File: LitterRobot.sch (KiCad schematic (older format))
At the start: 4 parts, among them J1 DF11C-4DP-2V(57), J2 Hirose_DF11C-6DP-2V(57), J3 DF11C-8DP-2V(57), J4 DF11C-10DP-2V(57)

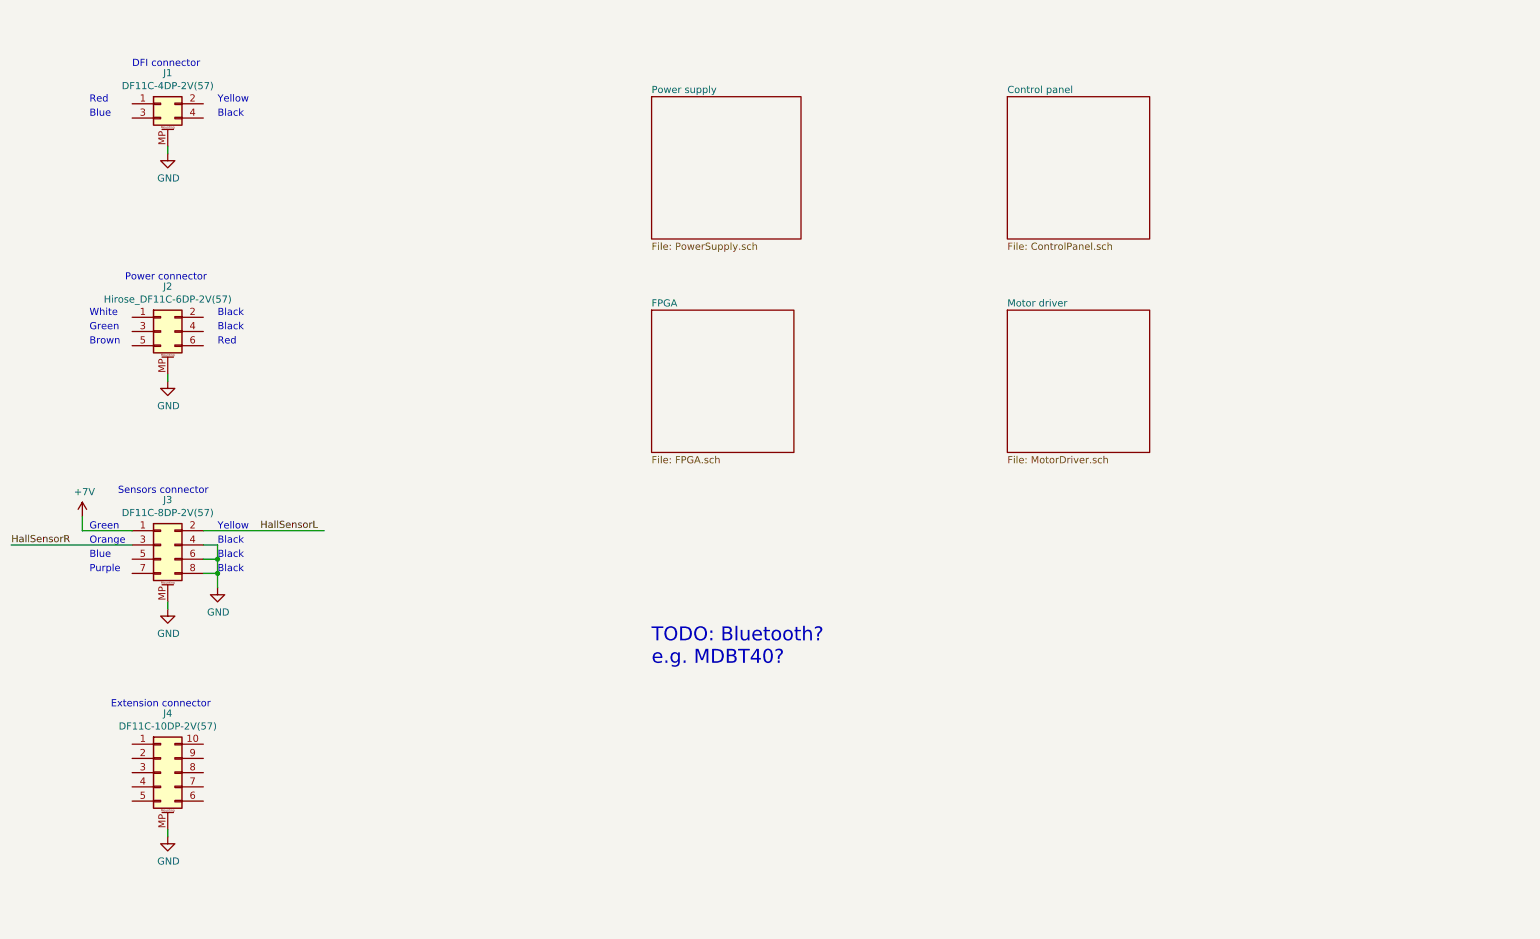
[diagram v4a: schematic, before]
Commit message: Add the power supply and motor driver ICs
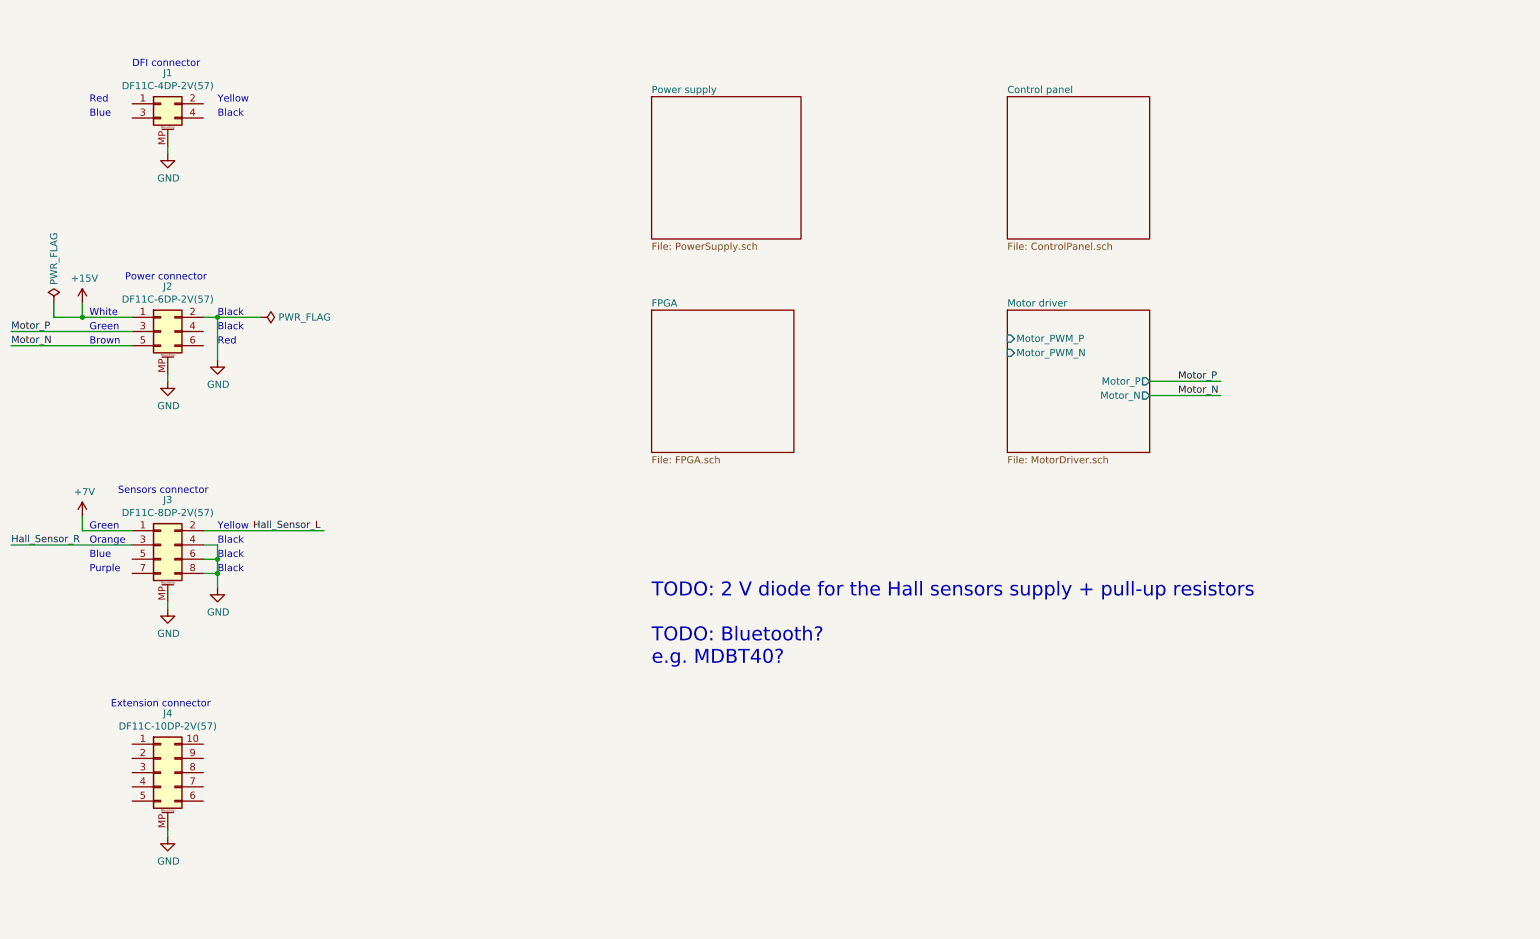
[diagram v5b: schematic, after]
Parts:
- J1: Part_Number (none) -> DF11C-4DP-2V(57)
- J2: value Hirose_DF11C-6DP-2V(57) -> DF11C-6DP-2V(57); Part_Number (none) -> DF11C-6DP-2V(57)
- J3: Part_Number (none) -> DF11C-8DP-2V(57)
- J4: Part_Number (none) -> DF11C-10DP-2V(57)
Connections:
- net labels added: +15V, Hall_Sensor_L, Hall_Sensor_R, Motor_N, Motor_P
- net labels removed: HallSensorL, HallSensorR
- wire segments 14 -> 25
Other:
- note added: "TODO: 2 V diode for the Hall sensors supply + pull-up resistors\n\nTODO: Bluetooth?\ne.g. MDBT40?"
- note removed: "TODO: Bluetooth?\ne.g. MDBT40?"
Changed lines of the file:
@@
 P 2050 3150
 F 0 "J2" H 2100 3467 50  0000 C CNN
-F 1 "Hirose_DF11C-6DP-2V(57)" H 2100 3376 50  0000 C CNN
+F 1 "DF11C-6DP-2V(57)" H 2100 3376 50  0000 C CNN
 F 2 "LitterRobot:Hirose_DF11C-6DP-2V(57)" H 2050 3150 50  0001 C CNN
 F 3 "https://www.hirose.com/en/product/document?clcode=CL0543-0683-4-57&productname=DF11C-6DP-2V(57)&series=DF11&documenttype=2DDrawing&lang=en&documentid=0000926113" H 2050 3150 50  0001 C CNN
+F 4 "DF11C-6DP-2V(57)" H 2050 3150 50  0001 C CNN "Part_Number"
 	1    2050 3150
 	1    0    0    -1
@@
 F 2 "LitterRobot:Hirose_DF11C-8DP-2V(57)" H 2050 4650 50  0001 C CNN
 F 3 "https://www.hirose.com/en/product/document?clcode=CL0543-0684-7-57&productname=DF11C-8DP-2V(57)&series=DF11&documenttype=2DDrawing&lang=en&documentid=0000999153" H 2050 4650 50  0001 C CNN
+F 4 "DF11C-8DP-2V(57)" H 2050 4650 50  0001 C CNN "Part_Number"
 	1    2050 4650
 	1    0    0    -1
@@
 	2100 1850 2100 1900
 $Comp
-L power:GND #PWR0101
+L power:GND #PWR03
 U 1 1 603BD2EA
 P 2100 1900
-F 0 "#PWR0101" H 2100 1650 50  0001 C CNN
+F 0 "#PWR03" H 2100 1650 50  0001 C CNN
 F 1 "GND" H 2105 1727 50  0000 C CNN
 F 2 "" H 2100 1900 50  0001 C CNN
@@
 F 2 "LitterRobot:Hirose_DF11C-4DP-2V(57)" H 2050 1550 50  0001 C CNN
 F 3 "https://www.hirose.com/en/product/document?clcode=CL0543-0682-1-57&productname=DF11C-4DP-2V(57)&series=DF11&documenttype=2DDrawing&lang=en&documentid=0000926110" H 2050 1550 50  0001 C CNN
+F 4 "DF11C-4DP-2V(57)" H 2050 1550 50  0001 C CNN "Part_Number"
 	1    2050 1550
 	1    0    0    -1
@@
 	2100 3450 2100 3500
 $Comp
-L power:GND #PWR0102
+L power:GND #PWR04
 U 1 1 603C0906
 P 2100 3500
-F 0 "#PWR0102" H 2100 3250 50  0001 C CNN
+F 0 "#PWR04" H 2100 3250 50  0001 C CNN
 F 1 "GND" H 2105 3327 50  0000 C CNN
 F 2 "" H 2100 3500 50  0001 C CNN
@@
 	2100 5050 2100 5100
 $Comp
-L power:GND #PWR0103
+L power:GND #PWR05
 U 1 1 603C0C1B
 P 2100 5100
-F 0 "#PWR0103" H 2100 4850 50  0001 C CNN
+F 0 "#PWR05" H 2100 4850 50  0001 C CNN
 F 1 "GND" H 2105 4927 50  0000 C CNN
 F 2 "" H 2100 5100 50  0001 C CNN
@@
 Black
 $Comp
-L power:GND #PWR0104
+L power:GND #PWR08
 U 1 1 603D1C90
 P 2450 4950
-F 0 "#PWR0104" H 2450 4700 50  0001 C CNN
+F 0 "#PWR08" H 2450 4700 50  0001 C CNN
 F 1 "GND" H 2455 4777 50  0000 C CNN
 F 2 "" H 2450 4950 50  0001 C CNN
@@
 	1850 4650 1000 4650
 Text Label 1000 4650 0    50   ~ 0
-HallSensorR
+Hall_Sensor_R
 Wire Wire Line
 	3200 4550 2350 4550
-Text Label 2750 4550 0    50   ~ 0
-HallSensorL
+Text Label 2700 4550 0    50   ~ 0
+Hall_Sensor_L
 Wire Wire Line
 	1850 4550 1500 4550
@@
 $EndSheet
 $Comp
-L LitterRobot:+7V #PWR?
+L LitterRobot:+7V #PWR02
 U 1 1 60414DA6
 P 1500 4450
-F 0 "#PWR?" H 1500 4300 50  0001 C CNN
+F 0 "#PWR02" H 1500 4300 50  0001 C CNN
 F 1 "+7V" H 1515 4623 50  0000 C CNN
 F 2 "" H 1500 4450 50  0001 C CNN
@@
 F 2 "LitterRobot:Hirose_DF11C-10DP-2V(57)" H 2050 6250 50  0001 C CNN
 F 3 "~" H 2050 6250 50  0001 C CNN
+F 4 "DF11C-10DP-2V(57)" H 2050 6250 50  0001 C CNN "Part_Number"
 	1    2050 6250
 	1    0    0    -1
@@
 	2100 6650 2100 6700
 $Comp
-L power:GND #PWR?
+L power:GND #PWR06
 U 1 1 603F0326
 P 2100 6700
-F 0 "#PWR?" H 2100 6450 50  0001 C CNN
+F 0 "#PWR06" H 2100 6450 50  0001 C CNN
 F 1 "GND" H 2105 6527 50  0000 C CNN
 F 2 "" H 2100 6700 50  0001 C CNN
@@
 F0 "Motor driver" 50
 F1 "MotorDriver.sch" 50
+F2 "Motor_PWM_P" I L 8000 3200 50
+F3 "Motor_PWM_N" I L 8000 3300 50
+F4 "Motor_P" O R 9000 3500 50
+F5 "Motor_N" O R 9000 3600 50
 $EndSheet
 Text Notes 5500 5500 0    98   ~ 0
-TODO: Bluetooth?\ne.g. MDBT40?
+TODO: 2 V diode for the Hall sensors supply + pull-up resistors\n\nTODO: Bluetooth?\ne.g. MDBT40?
+Wire Wire Line
+	1850 3050 1500 3050
+Wire Wire Line
+	1500 3050 1500 2950
+$Comp
+L power:+15V #PWR01
+U 1 1 6046C18F
+P 1500 2950
+F 0 "#PWR01" H 1500 2800 50  0001 C CNN
+F 1 "+15V" H 1515 3123 50  0000 C CNN
+F 2 "" H 1500 2950 50  0001 C CNN
+F 3 "" H 1500 2950 50  0001 C CNN
+	1    1500 2950
+	1    0    0    -1
+$EndComp
+Wire Wire Line
+	2350 3050 2450 3050
+Wire Wire Line
+	2450 3050 2450 3350
+$Comp
+L power:GND #PWR07
+U 1 1 6046CCE3
+P 2450 3350
+F 0 "#PWR07" H 2450 3100 50  0001 C CNN
+F 1 "GND" H 2455 3177 50  0000 C CNN
+F 2 "" H 2450 3350 50  0001 C CNN
+F 3 "" H 2450 3350 50  0001 C CNN
+	1    2450 3350
+	1    0    0    -1
+$EndComp
+Wire Wire Line
+	1000 3150 1850 3150
+Wire Wire Line
+	1000 3250 1850 3250
+Text Label 1000 3150 0    50   ~ 0
+Motor_P
+Text Label 1000 3250 0    50   ~ 0
+Motor_N
+$Comp
+L power:PWR_FLAG #FLG01
+U 1 1 60470C32
+P 1300 2950
+F 0 "#FLG01" H 1300 3025 50  0001 C CNN
+F 1 "PWR_FLAG" V 1300 3077 50  0000 L CNN
+F 2 "" H 1300 2950 50  0001 C CNN
+F 3 "~" H 1300 2950 50  0001 C CNN
+	1    1300 2950
+	1    0    0    -1
+$EndComp
+$Comp
+L power:PWR_FLAG #FLG02
+U 1 1 60471B9C
+P 2750 3050
+F 0 "#FLG02" H 2750 3125 50  0001 C CNN
+F 1 "PWR_FLAG" V 2750 3178 50  0000 L CNN
+F 2 "" H 2750 3050 50  0001 C CNN
+F 3 "~" H 2750 3050 50  0001 C CNN
+	1    2750 3050
+	0    1    1    0
+$EndComp
+Wire Wire Line
+	2750 3050 2450 3050
+Connection ~ 2450 3050
+Wire Wire Line
+	1500 3050 1300 3050
+Wire Wire Line
+	1300 3050 1300 2950
+Connection ~ 1500 3050
+Wire Wire Line
+	9000 3500 9500 3500
+Wire Wire Line
+	9000 3600 9500 3600
+Text Label 9200 3500 0    50   ~ 0
+Motor_P
+Text Label 9200 3600 0    50   ~ 0
+Motor_N
 $EndSCHEMATC

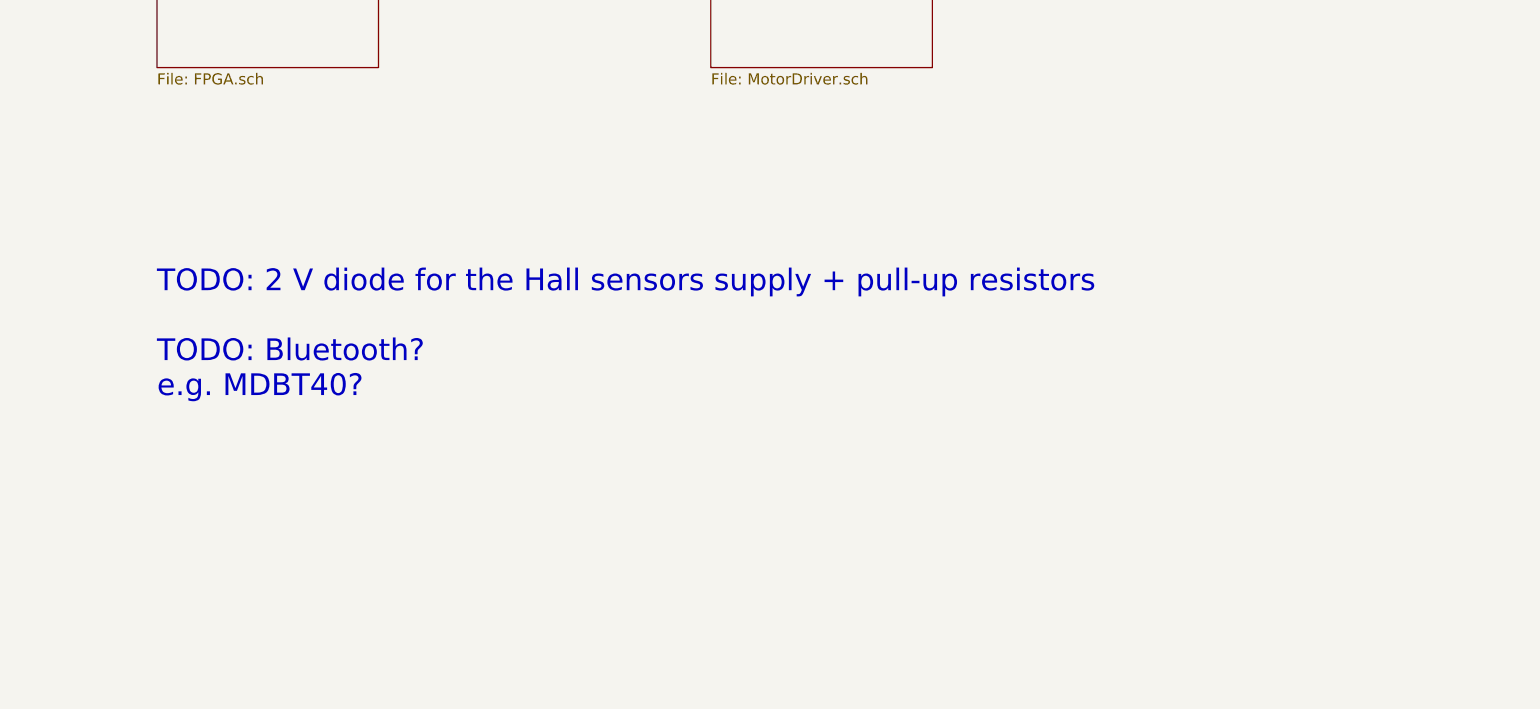
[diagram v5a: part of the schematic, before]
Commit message: Add the push buttons and mounting holes
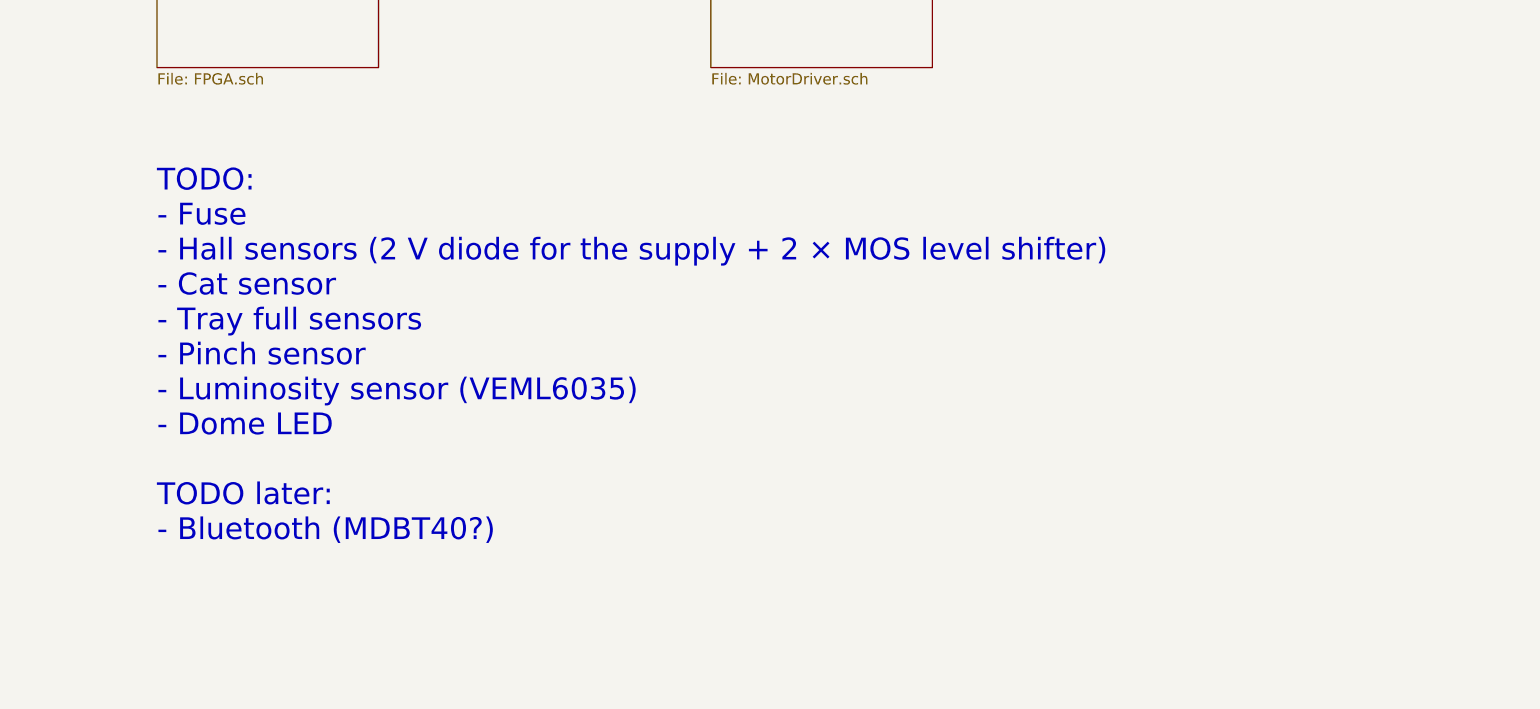
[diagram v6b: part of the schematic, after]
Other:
- note added: "TODO:\n- Fuse\n- Hall sensors (2 V diode for the supply + 2 × MOS level shifter)\n- Cat sensor\n- Tray full sensors\n- Pinch sensor\n- Luminosity sensor (VEML6035)\n- Dome LED\n\nTODO later:\n- Bluetooth (MDBT40?)"
- note removed: "TODO: 2 V diode for the Hall sensors supply + pull-up resistors\n\nTODO: Bluetooth?\ne.g. MDBT40?"
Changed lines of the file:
@@
 F5 "Motor_N" O R 9000 3600 50
 $EndSheet
-Text Notes 5500 5500 0    98   ~ 0
-TODO: 2 V diode for the Hall sensors supply + pull-up resistors\n\nTODO: Bluetooth?\ne.g. MDBT40?
+Text Notes 5500 6150 0    98   ~ 0
+TODO:\n- Fuse\n- Hall sensors (2 V diode for the supply + 2 × MOS level shifter)\n- Cat sensor\n- Tray full sensors\n- Pinch sensor\n- Luminosity sensor (VEML6035)\n- Dome LED\n\nTODO later:\n- Bluetooth (MDBT40?)
 Wire Wire Line
 	1850 3050 1500 3050

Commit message: Place the main components on the PCB
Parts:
- removed J4: DF11C-10DP-2V(57), LitterRobot:Hirose_DF11C-10DP-2V(57), symbol Connector_Generic_MountingPin:Conn_02x05_Counter_Clockwise_MountingPin
- added J4: DF11C-6DP-2V(57), LitterRobot:Hirose_DF11C-6DP-2V(57), symbol Connector_Generic_MountingPin:Conn_02x03_Odd_Even_MountingPin
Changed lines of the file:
@@
-	1    0    0    -1
-$EndComp
-$Comp
-L Connector_Generic_MountingPin:Conn_02x05_Counter_Clockwise_MountingPin J4
-U 1 1 603E9ABF
-P 2050 6250
-F 0 "J4" H 2100 6667 50  0000 C CNN
-F 1 "DF11C-10DP-2V(57)" H 2100 6576 50  0000 C CNN
-F 2 "LitterRobot:Hirose_DF11C-10DP-2V(57)" H 2050 6250 50  0001 C CNN
-F 3 "~" H 2050 6250 50  0001 C CNN
-F 4 "DF11C-10DP-2V(57)" H 2050 6250 50  0001 C CNN "Part_Number"
-	1    2050 6250
 	1    0    0    -1
 $EndComp
 Wire Wire Line
-	2100 6650 2100 6700
+	2100 6450 2100 6500
 $Comp
 L power:GND #PWR06
 U 1 1 603F0326
-P 2100 6700
-F 0 "#PWR06" H 2100 6450 50  0001 C CNN
-F 1 "GND" H 2105 6527 50  0000 C CNN
-F 2 "" H 2100 6700 50  0001 C CNN
-F 3 "" H 2100 6700 50  0001 C CNN
-	1    2100 6700
+P 2100 6500
+F 0 "#PWR06" H 2100 6250 50  0001 C CNN
+F 1 "GND" H 2105 6327 50  0000 C CNN
+F 2 "" H 2100 6500 50  0001 C CNN
+F 3 "" H 2100 6500 50  0001 C CNN
+	1    2100 6500
 	1    0    0    -1
 $EndComp
@@
 Text Label 9200 3600 0    50   ~ 0
 Motor_N
+$Comp
+L Connector_Generic_MountingPin:Conn_02x03_Odd_Even_MountingPin J4
+U 1 1 6051969D
+P 2050 6150
+F 0 "J4" H 2100 6467 50  0000 C CNN
+F 1 "DF11C-6DP-2V(57)" H 2100 6376 50  0000 C CNN
+F 2 "LitterRobot:Hirose_DF11C-6DP-2V(57)" H 2050 6150 50  0001 C CNN
+F 3 "https://www.hirose.com/en/product/document?clcode=CL0543-0683-4-57&productname=DF11C-6DP-2V(57)&series=DF11&documenttype=2DDrawing&lang=en&documentid=0000926113" H 2050 6150 50  0001 C CNN
+F 4 "DF11C-6DP-2V(57)" H 2050 6150 50  0001 C CNN "Part_Number"
+	1    2050 6150
+	1    0    0    -1
+$EndComp
 $EndSCHEMATC
